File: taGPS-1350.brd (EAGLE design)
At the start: 35 x 76.4 mm, 84 parts, among them IC1 MSP430FR698X(1)80-PIN_PN, IC3 FT232RL

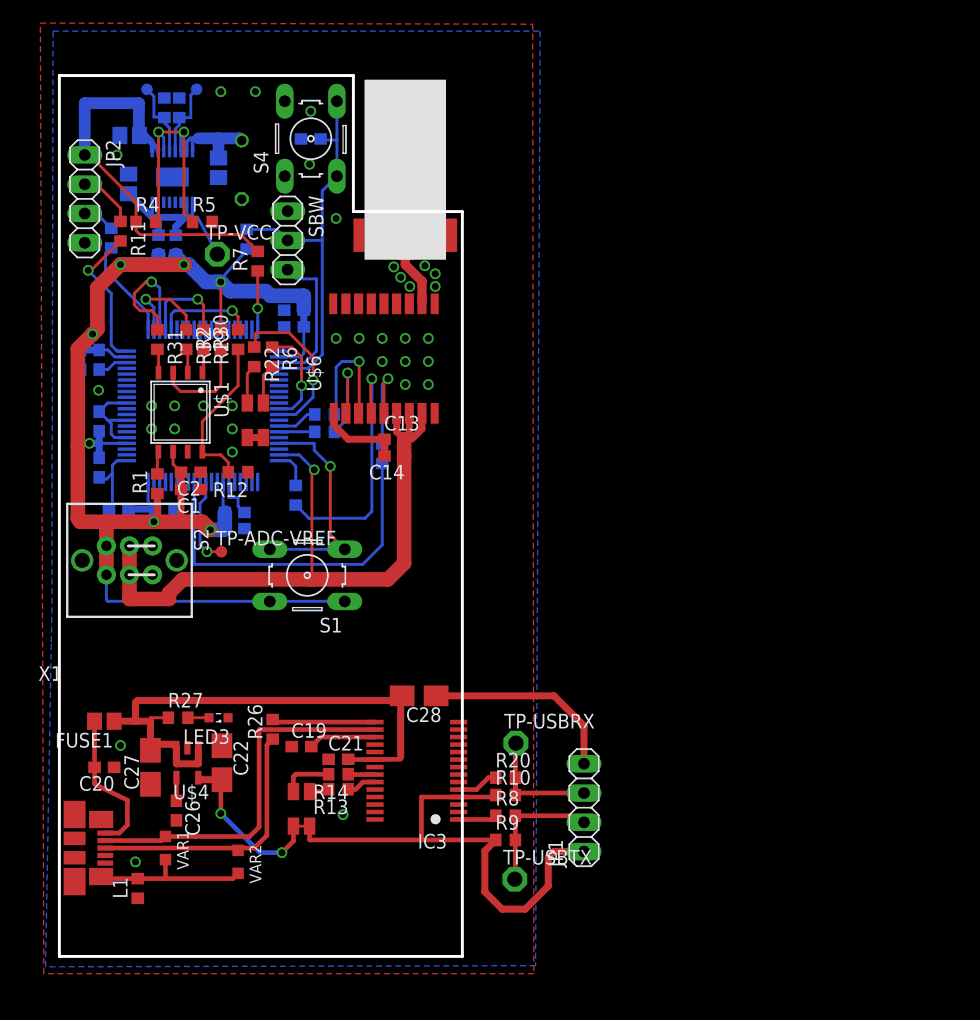
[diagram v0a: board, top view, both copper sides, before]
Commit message: Fix MCU RX/TX pinheader position, polish boards
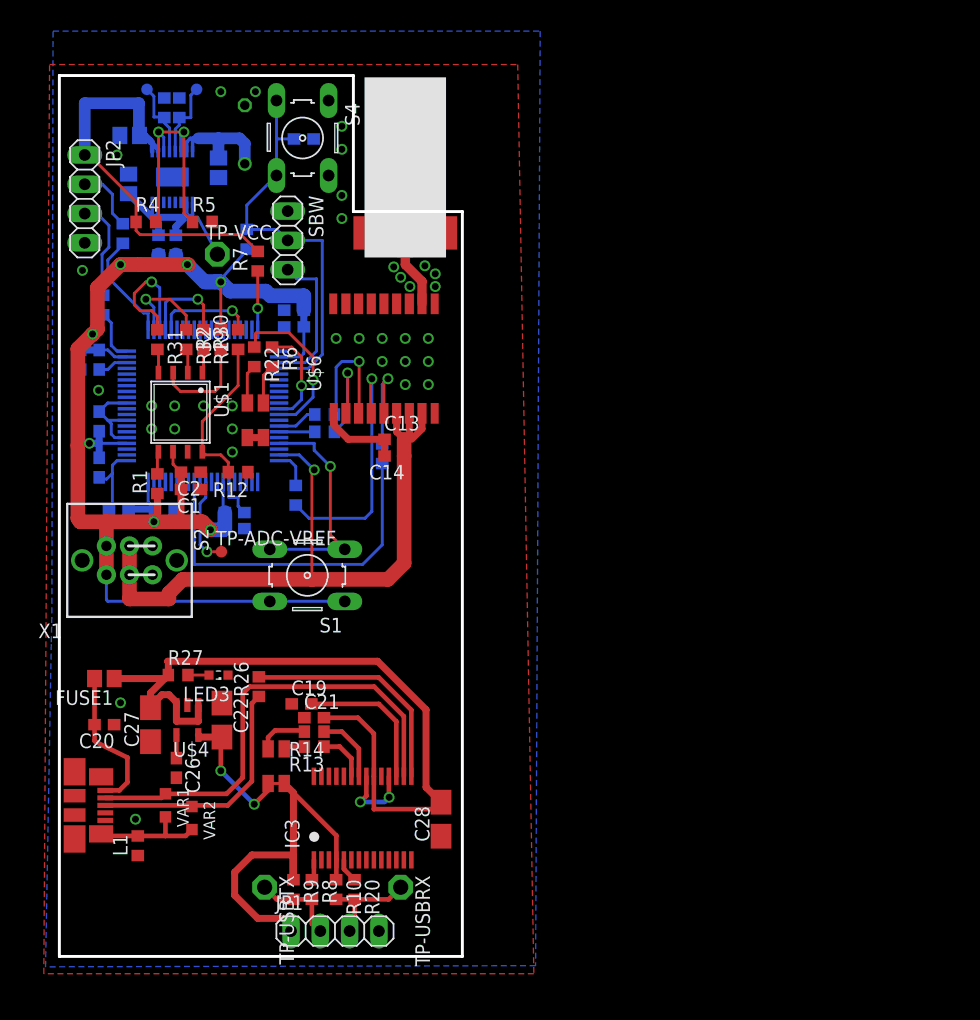
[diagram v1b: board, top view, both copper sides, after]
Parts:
- moved JP1 24.1 mm to (23.9, 2.20), turned to 0 degrees
- moved TP-USBTX 21.7 mm to (17.8, 6.00), turned to 270 degrees
- moved R9 18.9 mm to (20.3, 5.80), turned to 270 degrees
- moved R8 18.0 mm to (21.9, 5.80), turned to 270 degrees
- moved R10 16.8 mm to (24.0, 5.80), turned to 270 degrees
- moved R20 16.3 mm to (25.6, 5.80), turned to 270 degrees
- moved TP-USBRX 16.0 mm to (29.6, 6.00), turned to 270 degrees
- moved C28 10.9 mm to (33.1, 11.9), turned to 90 degrees
- moved R11 6.57 mm to (3.80, 56.5), flipped to the bottom
- moved IC3 6.24 mm to (26.3, 12.0), turned to 0 degrees
- moved VAR2 5.52 mm to (11.5, 12.0)
- moved LED2 4.30 mm to (18.8, 16.5)
- moved R13 4.25 mm to (22.1, 18.2)
- moved R14 4.25 mm to (22.1, 19.5)
- moved C21 4.17 mm to (22.1, 20.7)
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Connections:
- net MCU-TX-FT232: now also JP2.3; no longer JP2.2
- net N$8: now also JP2.2; no longer JP2.3
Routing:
- net VBUS: track 49.3 -> 67.3 mm
- net VCCUSB: track 61.5 -> 47.7 mm
- net N$29: track 8.97 -> 20.2 mm
- net GND: track 47.7 -> 37.4 mm, vias 33 -> 37
- net N$2: track 12.7 -> 4.50 mm, vias 1 -> 0
- net N$13: track 32.3 -> 40.4 mm
- net N$10: track 5.87 -> 12.8 mm
- net FT232-TX: track 11.7 -> 7.62 mm
- net N$23: track 13.8 -> 9.83 mm
- net MCU-TX-FT232: track 5.11 -> 8.87 mm
- net N$17: track 2.36 -> 6.04 mm
- net FT232-RX: track 12.0 -> 8.96 mm
- net N$8: track 2.83 -> 5.68 mm
- net VCC: track 140.8 -> 143.1 mm
- net VCC_BATT_IN: track 8.67 -> 10.8 mm
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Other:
- board text added: "GND TX RX VCC"
- board text added: "VCC - TX - RX - GND"
- board text removed: "RX-USB-TX"
- board text removed: "VCC"

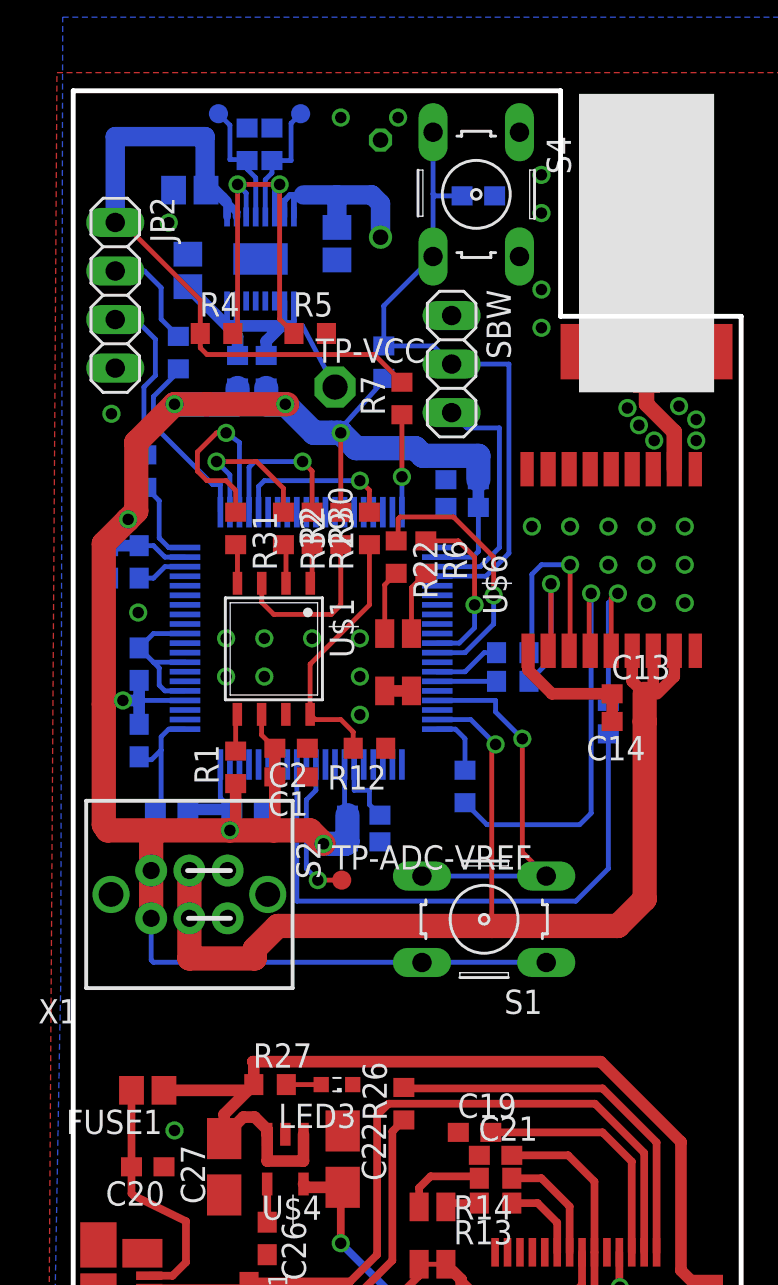
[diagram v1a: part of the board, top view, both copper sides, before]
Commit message: Replace FUSE package to 1812
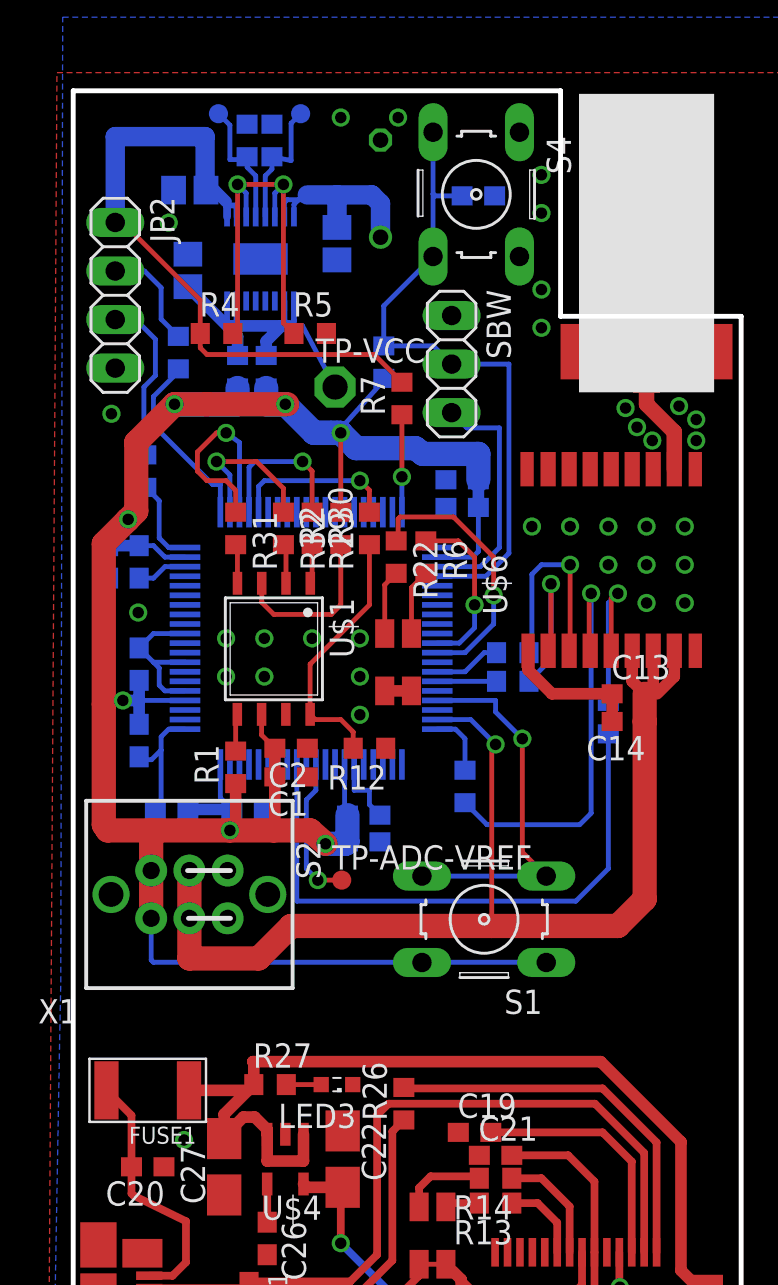
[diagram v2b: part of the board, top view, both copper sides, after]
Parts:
- FUSE1: value 500mA -> SMD1206R500SF; device tagps:R0805 -> tagps:F1812
- moved R15 0.20 mm to (10.4, 73.8)
- moved R16 0.20 mm to (9.10, 73.8)
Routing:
- net N$7: track 23.8 -> 22.1 mm
- net VBUS: track 67.3 -> 66.0 mm
- net N$22: track 13.0 -> 13.5 mm

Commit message: Check rules acc seeed studio
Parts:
- moved R10 0.50 mm to (23.5, 5.80)
- moved R20 0.50 mm to (25.1, 5.80)
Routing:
- net GND: track 37.4 -> 40.6 mm, vias 37 -> 50
- net FT232-RX: track 8.96 -> 9.52 mm

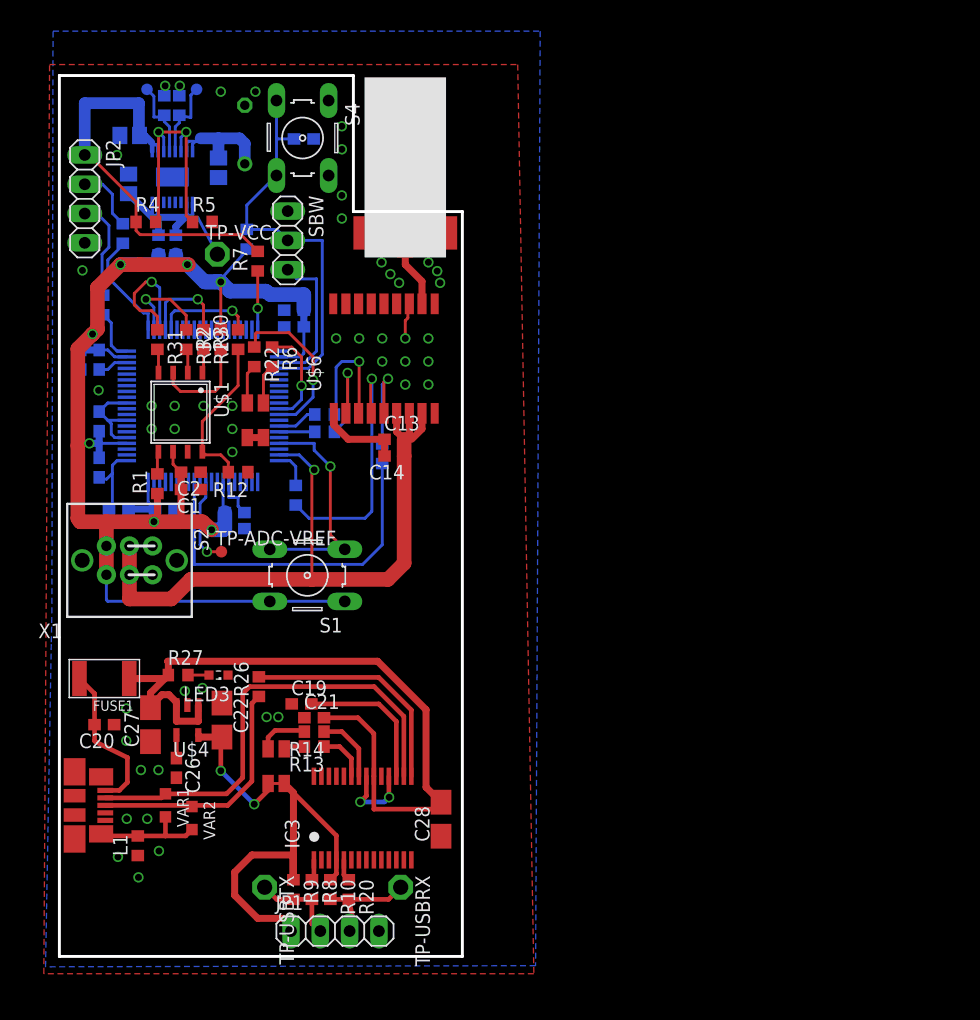
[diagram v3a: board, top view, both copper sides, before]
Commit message: Redesign type 1350 to get wider copper plane for antenna
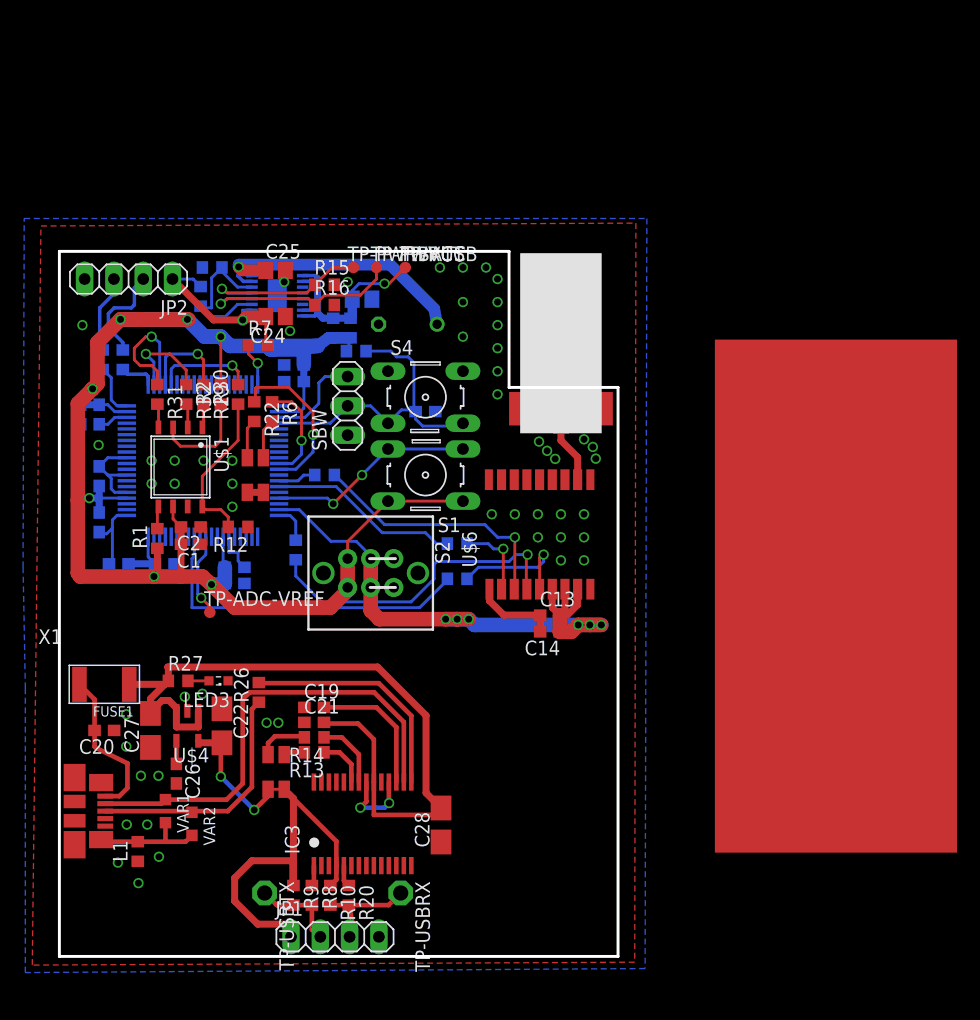
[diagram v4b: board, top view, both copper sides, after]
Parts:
- TP-VCC: value TPSQPAD1-13 -> TPSQTP10R; device tagps:P1-13 -> tagps:TP10R
- moved C15 25.9 mm to (31.8, 47.2)
- moved TP-PWRUSB 25.2 mm to (27.5, 59.8), flipped to the top
- moved S4 24.9 mm to (31.8, 48.5), turned to 0 degrees
- moved C18 22.6 mm to (26.2, 57.0), turned to 180 degrees
- moved R16 22.2 mm to (23.0, 56.5), flipped to the top, turned to 0 degrees
- moved G2 21.7 mm to (30.2, 54.8), turned to 0 degrees
- moved S2 20.9 mm to (27.0, 33.2)
- moved TP-PWRBATT 20.6 mm to (25.5, 59.8), flipped to the top
- moved U$5 20.4 mm to (43.5, 49.0)
- moved U$6 20.4 mm to (36.6, 41.5)
- moved C13 20.4 mm to (42.5, 29.6)
- moved C14 20.4 mm to (42.5, 28.1)
- moved C24 20.2 mm to (18.8, 55.5), flipped to the top
- moved R15 20.0 mm to (23.0, 58.2), flipped to the top, turned to 0 degrees
- moved R18 18.1 mm to (25.2, 54.5)
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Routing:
- net VCCUSBGPS: track 35.2 -> 17.7 mm, vias 0 -> 1
- net VCC_BATT_IN: track 10.6 -> 26.7 mm, vias 0 -> 1
- net N$45: track 3.10 -> 16.7 mm
- net N$25: track 6.99 -> 18.7 mm, vias 0 -> 1
- net MB-GPS-RX: track 10.9 -> 22.4 mm
- net MB-PWR_GPS_SENSE: track 61.9 -> 50.4 mm, vias 1 -> 6
- net N$7: track 22.1 -> 13.7 mm, vias 2 -> 0
- net ADC-BATT: track 6.97 -> 15.2 mm, vias 0 -> 1
- net VCC: track 143.1 -> 150.9 mm
- net SBW-TDO/TDI: track 34.9 -> 27.4 mm
- net MCU-RX-FT232: track 9.72 -> 3.15 mm
- net N$47: track 21.9 -> 27.9 mm
- net SBW-TCK: track 12.8 -> 8.47 mm
- net N$8: track 5.68 -> 8.80 mm
- net GND: track 40.6 -> 37.6 mm, vias 50 -> 55
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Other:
- board size 35 x 76.4 mm -> 48.5 x 61.1 mm
- board text added: "GND-RST-TST"
- board text added: "VCC"
- board text removed: "TST-RST-GND"

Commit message: Fix antenna position, grounding
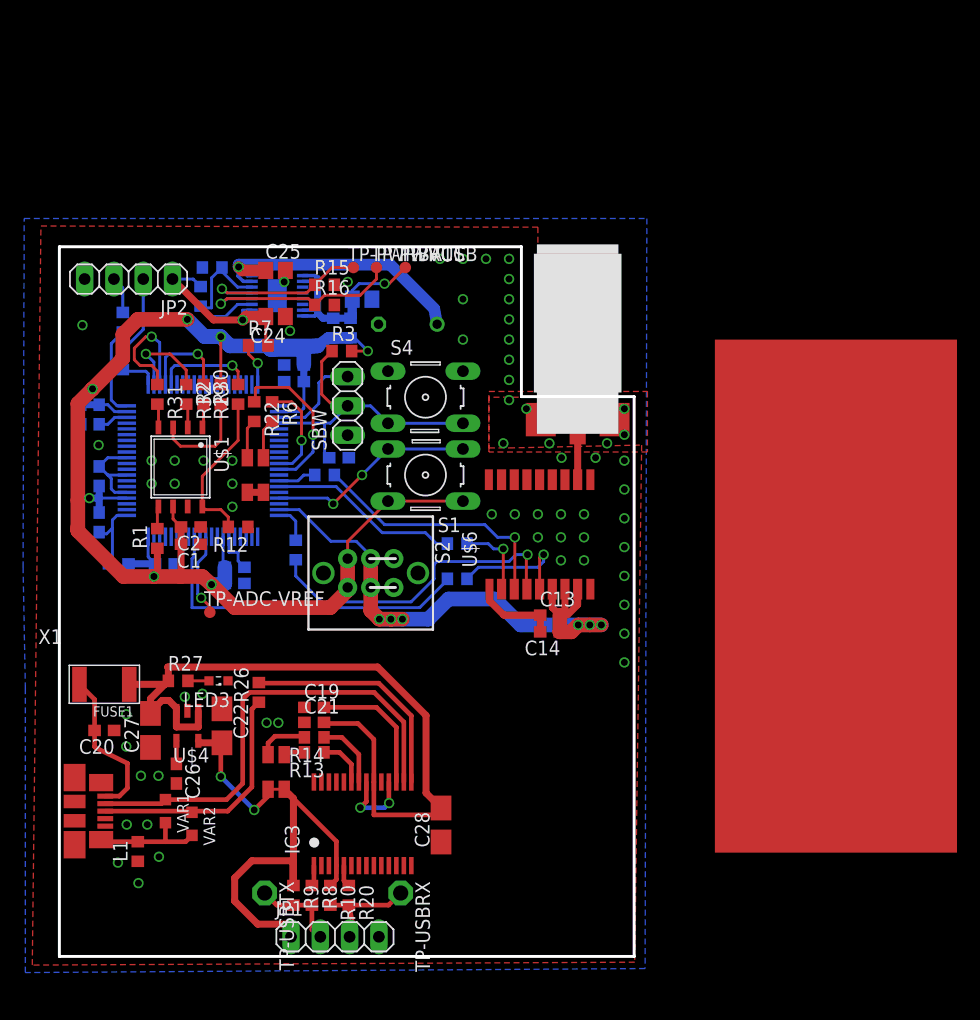
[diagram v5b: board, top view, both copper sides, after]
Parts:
- moved C15 8.50 mm to (24.2, 43.2)
- moved R11 3.69 mm to (5.50, 55.0)
- moved U$5 1.73 mm to (45.0, 48.0)
- moved R3 1.25 mm to (24.5, 52.5), flipped to the top
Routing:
- net VCC: track 150.9 -> 139.4 mm
- net MCU-TX-FT232: track 6.76 -> 3.22 mm
- net N$2: track 4.53 -> 7.87 mm
- net N$27: track 7.00 -> 4.76 mm
- net N$8: track 8.80 -> 6.88 mm
- net MB-PWR_GPS_SENSE: track 50.4 -> 51.9 mm
- net GND: vias 55 -> 71
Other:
- board size 48.5 x 61.1 mm -> 49.9 x 61.5 mm
